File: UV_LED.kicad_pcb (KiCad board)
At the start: 2 copper layers, 132.7 x 82.5 mm, 64 parts, among them IC1 ATMEGA328P-A, P1 12Vin, P2 USB_A, P3 CONN_01X16, P4 VACUUM, P5 LED_TOP, P6 LED_BOTTOM, Q1 MOSFET_N, Q2 MOSFET_N, Q3 MOSFET_N, Q4 MMBT3906, SW1 SPST, U1 FT232RL, U2 ACT4060A, U3 MPXV6115V, U4 PCF8574, X1 16mHz

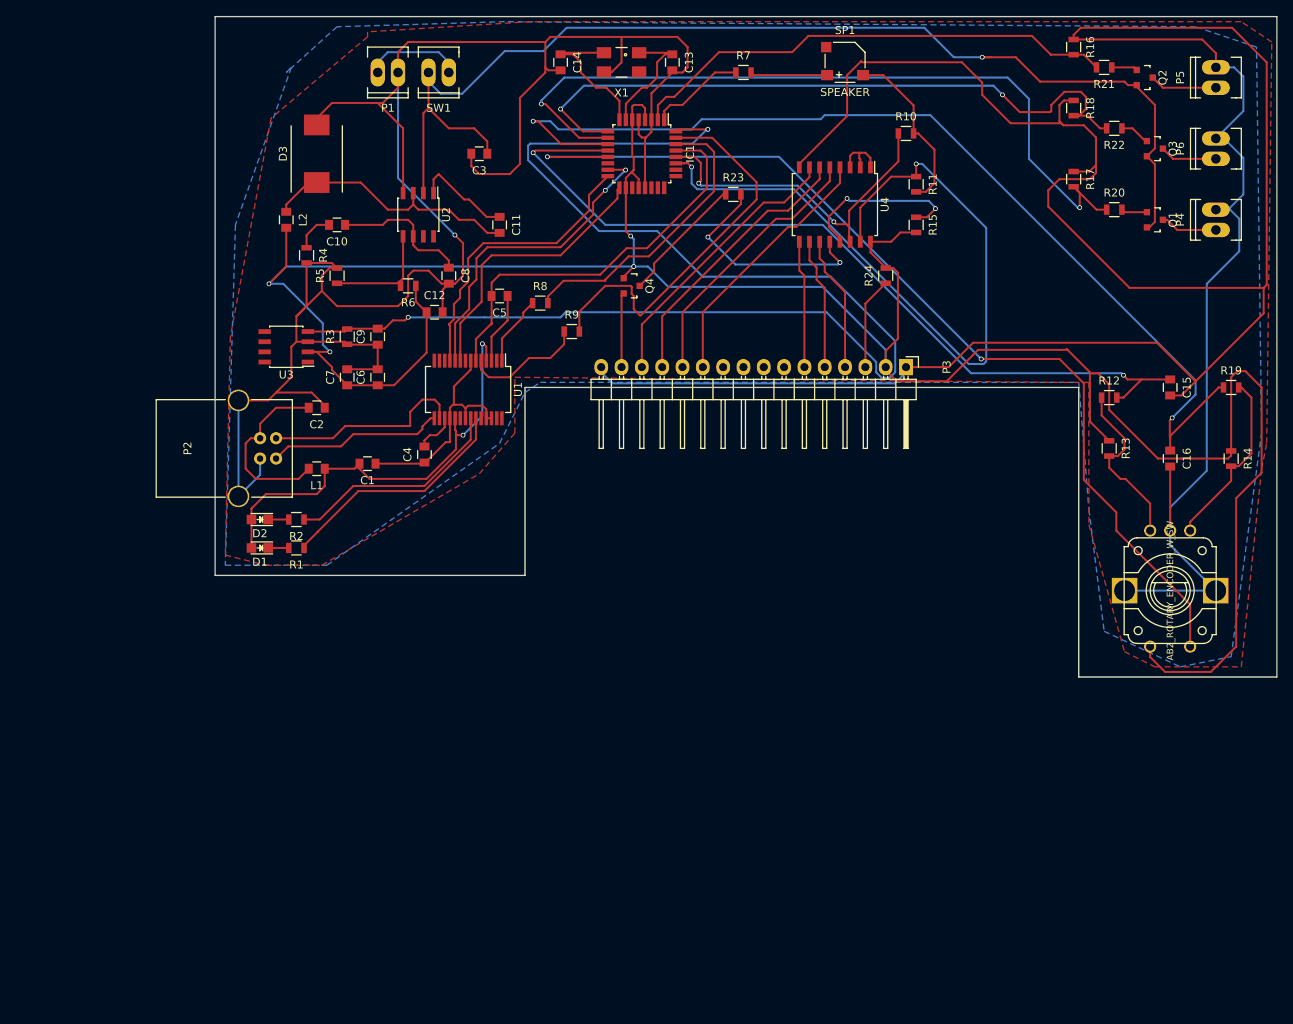
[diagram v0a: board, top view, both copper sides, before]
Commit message: schematic changes, new pcb
simplified the schematic, added reset button, remade pcb for easier
home processing
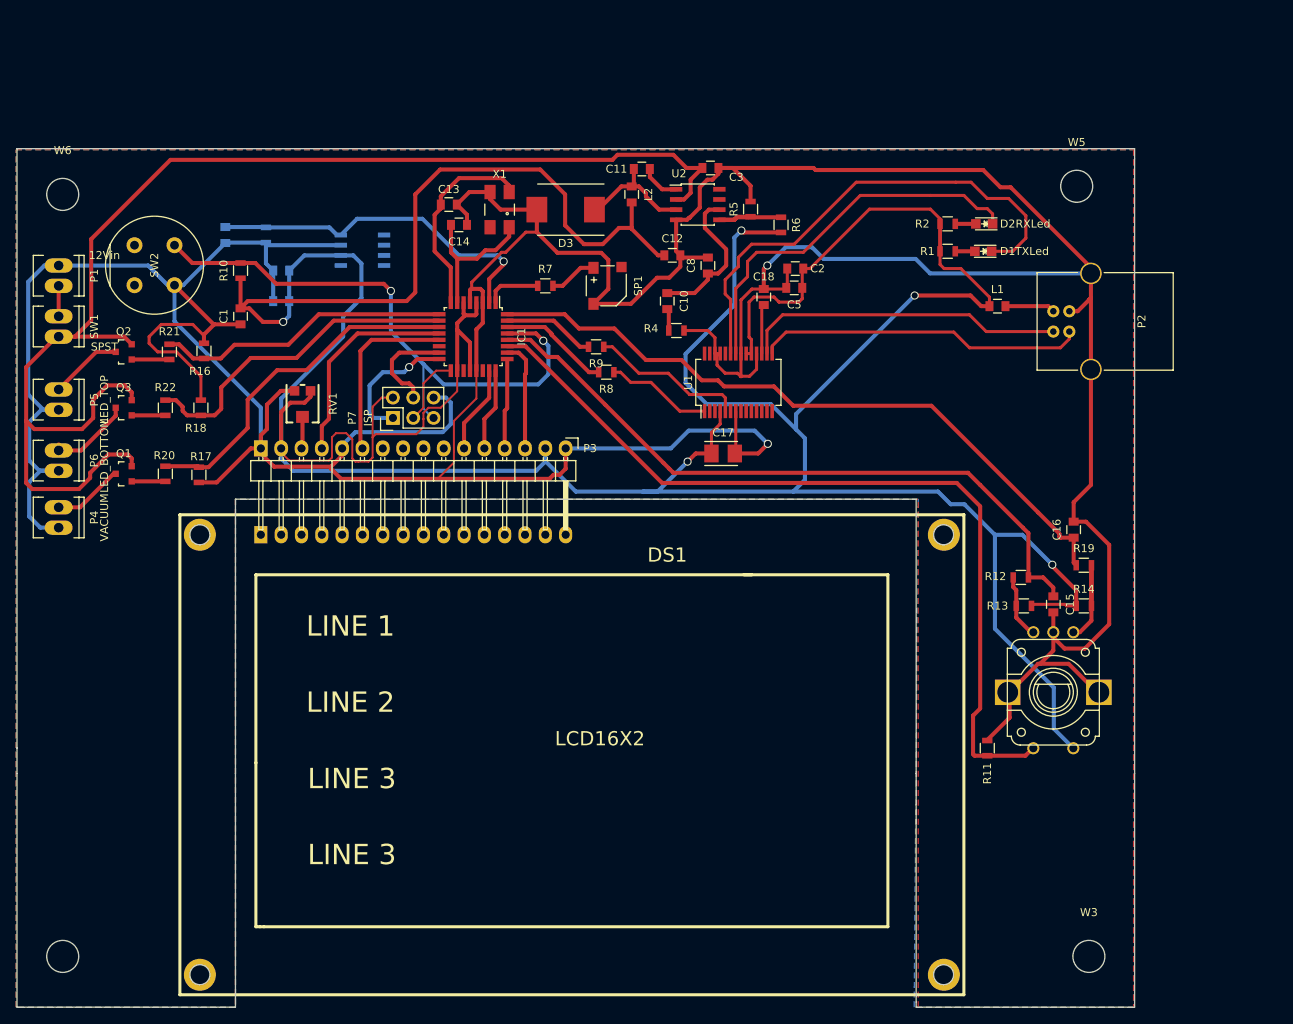
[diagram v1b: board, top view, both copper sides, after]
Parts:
- removed C4: 100nF, Capacitors_SMD:C_0805
- removed Q4: MMBT3906, TO_SOT_Packages_SMD:SOT-23
- removed R15, R24: 10k, Resistors_SMD:R_0805
- removed R23: 1k, Resistors_SMD:R_0805
- removed U4: PCF8574, Housings_SOIC:SOIC-16_7.5x10.3mm_Pitch1.27mm
- added C17: 10uF, Capacitors_Tantalum_SMD:TantalC_SizeB_EIA-3528_Reflow, F.Cu at (162.6, 88.3)
- added C18: 0.1uF, Capacitors_SMD:C_0805, F.Cu at (167.6, 68.7)
- added DS1: LCD16X2, Display:DISPLAY_4x20(16), F.Cu at (97.2, 98.4)
- added P7: ISP, Pin_Headers:Pin_Header_Straight_2x03, F.Cu at (121.3, 83.8)
- added RV1: 10k, TC33X-2-103E:35WR, F.Cu at (110.0, 82.0)
- added SW2: RESET, Buttons_Switches_ThroughHole:Push_E-Switch_KS01Q01, F.Cu at (94.0, 62.2)
- added W1: TEST_1P, Mounting_Holes:MountingHole_2-5mm, F.Cu at (190.1, 98.4)
- added W2: TEST_1P, Mounting_Holes:MountingHole_2-5mm, F.Cu at (97.2, 98.4)
- added W3: TEST_1P, Mounting_Holes:MountingHole_4mm, F.Cu at (208.3, 151.1)
- added W4: TEST_1P, Mounting_Holes:MountingHole_4mm, F.Cu at (80.0, 151.1)
- added W5: TEST_1P, Mounting_Holes:MountingHole_4mm, F.Cu at (206.8, 54.9)
- added W6: TEST_1P, Mounting_Holes:MountingHole_4mm, F.Cu at (80.0, 55.9)
- added W7: TEST_1P, Mounting_Holes:MountingHole_2-5mm, F.Cu at (97.2, 153.4)
- added W8: TEST_1P, Mounting_Holes:MountingHole_2-5mm, F.Cu at (190.1, 153.4)
- C2: value 10nF -> 0.1uF
- C6, C7, C9, R3, U3: moved to B.Cu
- P3: footprint Pin_Headers:Pin_Header_Angled_1x16 -> Display:Pin_Header_Angled_1x16_backward
- R1, R2: value 3.3k -> 330R
- R10: value 4.7k -> 10K
- R11: value 4.7k -> 10k
- moved P5 150.2 mm to (79.5, 81.5), turned to 270 degrees
- moved P6 149.8 mm to (79.5, 89.2), turned to 270 degrees
- moved P4 149.4 mm to (79.5, 96.3), turned to 270 degrees
- moved Q3 132.9 mm to (87.6, 82.5), turned to 90 degrees
- moved Q1 132.8 mm to (87.6, 90.8), turned to 90 degrees
- moved Q2 132.2 mm to (87.6, 75.6), turned to 90 degrees
- moved R22 123.7 mm to (92.8, 82.5), turned to 90 degrees
- moved R20 123.1 mm to (92.8, 90.8), turned to 270 degrees
- moved R21 122.1 mm to (93.3, 75.6), turned to 90 degrees
- moved R17 115.4 mm to (97.0, 90.9), turned to 90 degrees
- moved R18 115.3 mm to (97.3, 82.5)
- moved R16 115.2 mm to (97.7, 75.4)
- moved P2 98.9 mm to (203.8, 70.5), turned to 0 degrees
- moved D2 97.8 mm to (195.2, 59.6)
- moved D1 97.7 mm to (195.1, 63.0)
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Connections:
- C1 pad 1: Net-(C1-Pad1) -> GND
- C1 pad 2: Net-(C1-Pad2) -> /+5V
- C13 pad 1: Net-(C13-Pad1) -> GND
- C13 pad 2: GND -> Net-(C13-Pad2)
- C14 pad 1: Net-(C14-Pad1) -> GND
- C14 pad 2: GND -> Net-(C14-Pad2)
- C15 pad 2: Net-(C15-Pad2) -> GND
- C16 pad 2: Net-(C15-Pad2) -> GND
- C2 pad 1: GND -> /+5V
- C2 pad 2: Net-(C2-Pad2) -> GND
- C5 pad 1: Net-(C5-Pad1) -> /+5V
- C5 pad 2: Net-(C5-Pad2) -> GND
- D1 pad 2: Net-(C1-Pad2) -> Net-(D1-Pad2)
- D2 pad 2: Net-(C1-Pad2) -> Net-(D2-Pad2)
- IC1 pad 11: Net-(C16-Pad1) -> Net-(IC1-Pad11)
- IC1 pad 12: Net-(C15-Pad1) -> Net-(IC1-Pad12)
- IC1 pad 2: Net-(IC1-Pad2) -> Net-(C9-Pad2)
- IC1 pad 28: Net-(IC1-Pad28) -> Net-(C15-Pad1)
- IC1 pad 29: Net-(C5-Pad2) -> Net-(IC1-Pad29)
- IC1 pad 32: Net-(C9-Pad2) -> Net-(C16-Pad1)
- IC1 pad 7: Net-(C13-Pad1) -> Net-(C14-Pad2)
- IC1 pad 8: Net-(C14-Pad1) -> Net-(C13-Pad2)
- L1 pad 1: Net-(C1-Pad2) -> /+5V
- L1 pad 2: Net-(C2-Pad2) -> Net-(L1-Pad2)
- P2 pad 1: Net-(P2-Pad1) -> Net-(L1-Pad2)
- P2 pad 3: Net-(C2-Pad2) -> Net-(P2-Pad3)
- P3 pad 1: Net-(C15-Pad2) -> GND
- P3 pad 11: Net-(P3-Pad11) -> Net-(IC1-Pad23)
- P3 pad 12: Net-(P3-Pad12) -> Net-(IC1-Pad24)
- P3 pad 13: Net-(P3-Pad13) -> Net-(IC1-Pad25)
- P3 pad 14: Net-(P3-Pad14) -> Net-(IC1-Pad26)
- P3 pad 15: Net-(P3-Pad15) -> /+5V
- P3 pad 16: Net-(C15-Pad2) -> GND
- P3 pad 4: Net-(P3-Pad4) -> Net-(IC1-Pad12)
- P3 pad 5: Net-(P3-Pad5) -> GND
- P3 pad 6: Net-(P3-Pad6) -> Net-(IC1-Pad13)
- P4 pad 2: Net-(C15-Pad2) -> GND
- P5 pad 2: Net-(C15-Pad2) -> GND
- P6 pad 2: Net-(C15-Pad2) -> GND
- R1 pad 1: Net-(R1-Pad1) -> Net-(D1-Pad2)
- R1 pad 2: Net-(D1-Pad1) -> /+5V
- R10 pad 1: Net-(IC1-Pad28) -> /+5V
- R10 pad 2: Net-(R10-Pad2) -> Net-(IC1-Pad29)
- R11 pad 2: Net-(R10-Pad2) -> GND
- R16 pad 1: Net-(C15-Pad2) -> GND
- R16 pad 2: Net-(IC1-Pad2) -> Net-(IC1-Pad9)
- R17 pad 1: Net-(C15-Pad2) -> GND
- R17 pad 2: Net-(IC1-Pad10) -> Net-(IC1-Pad11)
- R18 pad 1: Net-(C15-Pad2) -> GND
- R18 pad 2: Net-(IC1-Pad9) -> Net-(IC1-Pad10)
- R2 pad 1: Net-(R2-Pad1) -> Net-(D2-Pad2)
- R2 pad 2: Net-(D2-Pad1) -> /+5V
- R20 pad 1: Net-(IC1-Pad10) -> Net-(IC1-Pad11)
- R21 pad 2: Net-(IC1-Pad2) -> Net-(IC1-Pad9)
- R22 pad 2: Net-(IC1-Pad9) -> Net-(IC1-Pad10)
- ROT_ENC1 pad 2: Net-(C15-Pad2) -> GND
- ROT_ENC1 pad 4: /+5V -> Net-(IC1-Pad27)
- ROT_ENC1 pad 6: Net-(IC1-Pad13) -> /+5V
- ROT_ENC1 pad 7: Net-(C15-Pad2) -> GND
- SP1 pad 2: Net-(R10-Pad2) -> GND
- U1 pad 10: Net-(IC1-Pad15) -> Net-(U1-Pad10)
- U1 pad 11: Net-(IC1-Pad16) -> Net-(U1-Pad11)
- U1 pad 15: Net-(P2-Pad1) -> Net-(P2-Pad3)
- U1 pad 18: Net-(C1-Pad1) -> GND
- U1 pad 19: Net-(C1-Pad2) -> /+5V
- U1 pad 20: Net-(C1-Pad2) -> /+5V
- U1 pad 21: Net-(C1-Pad1) -> GND
- U1 pad 22: Net-(R2-Pad1) -> Net-(D2-Pad1)
- U1 pad 23: Net-(R1-Pad1) -> Net-(D1-Pad1)
- U1 pad 25: Net-(C1-Pad1) -> GND
- U1 pad 26: Net-(C1-Pad1) -> GND
- U1 pad 3: Net-(C5-Pad1) -> Net-(U1-Pad3)
- U1 pad 4: Net-(C1-Pad2) -> /+5V
- U1 pad 6: Net-(C5-Pad2) -> Net-(U1-Pad6)
- U1 pad 7: Net-(C1-Pad1) -> GND
- U1 pad 9: Net-(IC1-Pad17) -> Net-(U1-Pad9)
- X1 pad 1: Net-(C13-Pad1) -> Net-(C14-Pad2)
- X1 pad 2: Net-(C14-Pad1) -> Net-(C13-Pad2)
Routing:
- net Net-(C15-Pad2): track 380.0 -> 0.00 mm
- net GND: track 256.7 -> 613.2 mm, vias 1 -> 2
- net /+5V: track 314.6 -> 514.0 mm, vias 4 -> 5
- net Net-(C9-Pad2): track 167.2 -> 44.2 mm, vias 2 -> 1
- net Net-(IC1-Pad13): track 124.8 -> 22.7 mm, vias 2 -> 0
- net Net-(IC1-Pad29): track 0.00 -> 74.1 mm, vias 0 -> 2
- net Net-(IC1-Pad2): track 61.9 -> 0.00 mm
- net Net-(D1-Pad1): track 2.57 -> 62.3 mm
- net Net-(C1-Pad2): track 56.5 -> 0.00 mm, vias 2 -> 0
- net Net-(IC1-Pad10): track 97.7 -> 41.8 mm, vias 2 -> 0
- net Net-(C5-Pad2): track 50.6 -> 0.00 mm
- net Net-(IC1-Pad9): track 85.6 -> 36.7 mm, vias 2 -> 0
- net Net-(D2-Pad1): track 2.57 -> 48.4 mm
- net Net-(IC1-Pad11): track 0.00 -> 43.6 mm
- net Net-(IC1-Pad28): track 43.3 -> 0.00 mm, vias 2 -> 0
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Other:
- board size 132.7 x 82.5 mm -> 139.7 x 107.3 mm

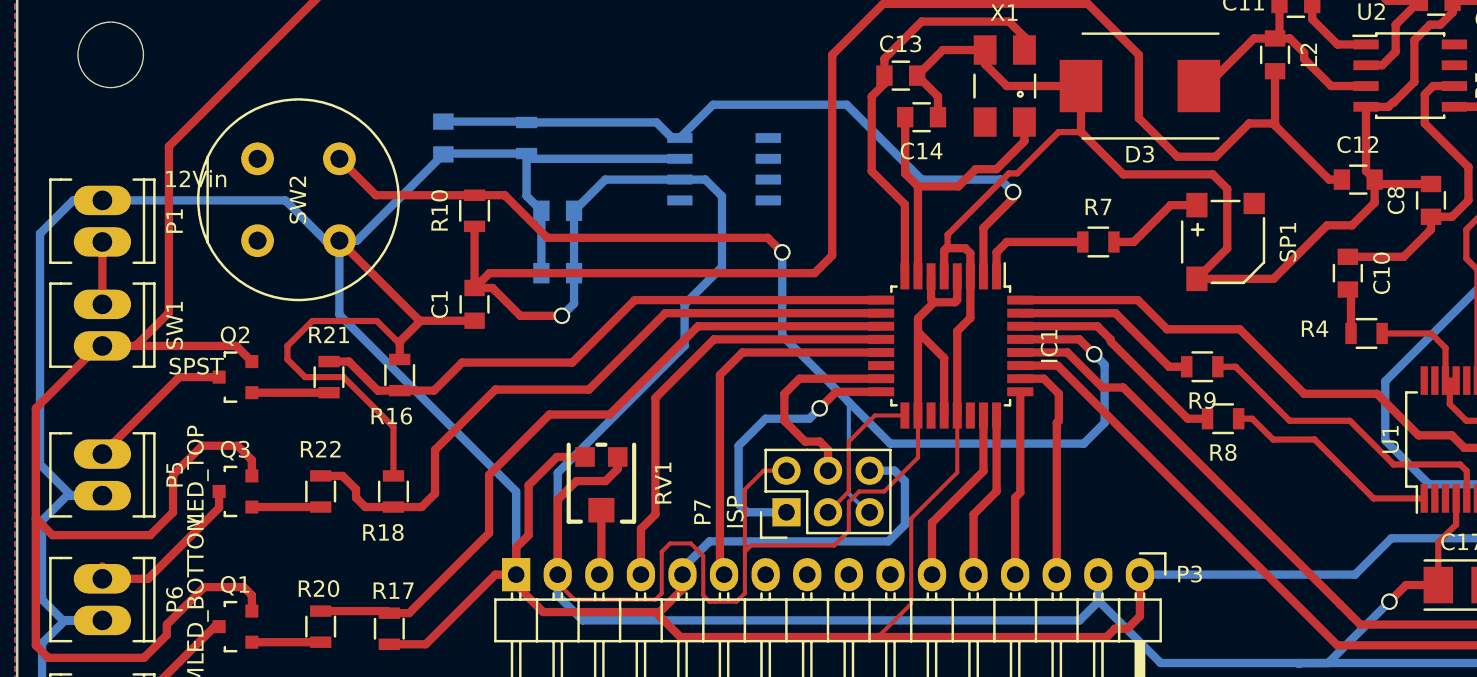
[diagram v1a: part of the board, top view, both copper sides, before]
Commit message: added renders, rerouted PCB
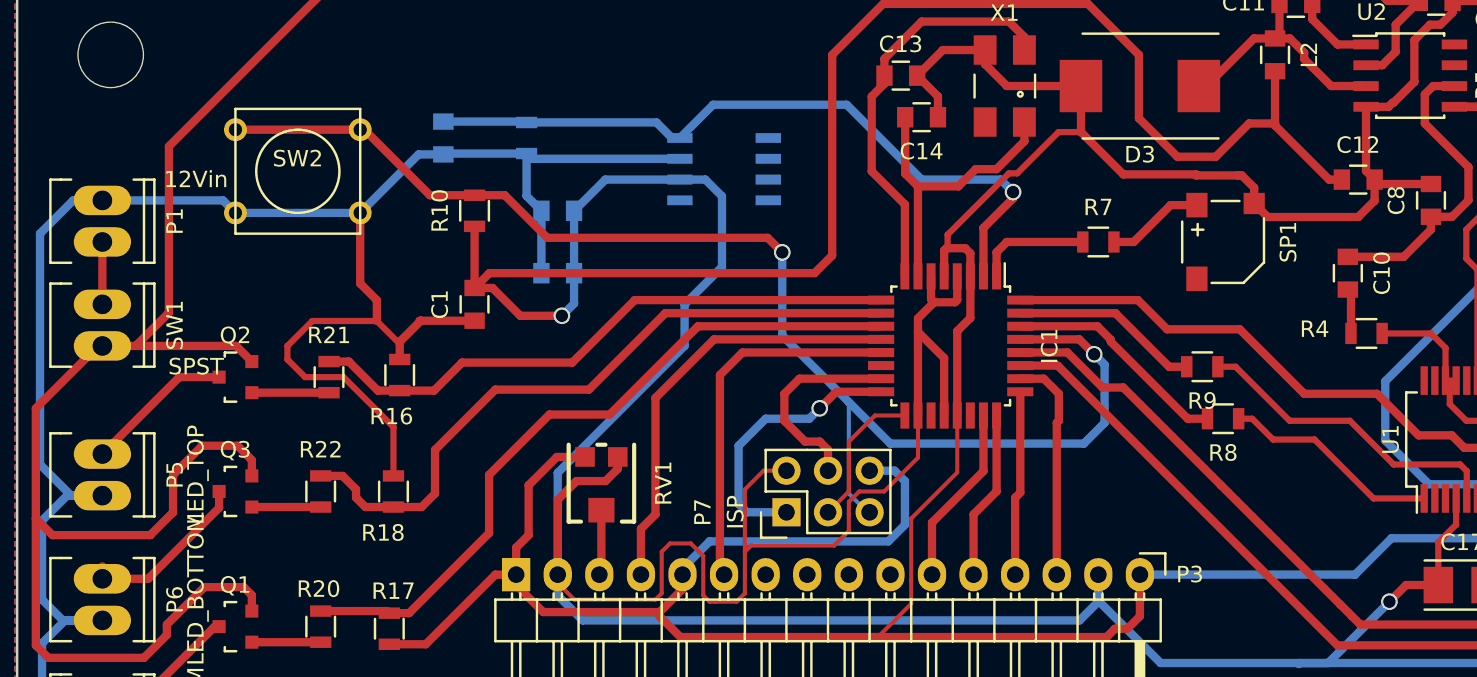
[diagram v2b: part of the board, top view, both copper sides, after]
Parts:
- SP1: footprint pui_transducer:SMT-0540-S-R -> Speakers:SMT-0540-S-R
- SW2: footprint Buttons_Switches_ThroughHole:Push_E-Switch_KS01Q01 -> Buttons_Switches_ThroughHole:SW_PUSH_SMALL
- moved SW2 2.65 mm to (91.4, 63.0), turned to 0 degrees
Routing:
- net GND: track 613.2 -> 578.5 mm
- net Net-(IC1-Pad29): track 74.1 -> 81.2 mm
